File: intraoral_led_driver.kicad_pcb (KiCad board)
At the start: 2 copper layers, 53.8 x 33.2 mm, 248 parts, among them J1 CONN_01X04, J2 CONN_01X03, J3 CONN_01X04, J4 CONN_01X02, J5 CONN_01X02, Q1 Si2318DS-T1, Q2 Si2318DS-T1, SW1 SW_SPST, U1 LT3478-1, U3 AD5247

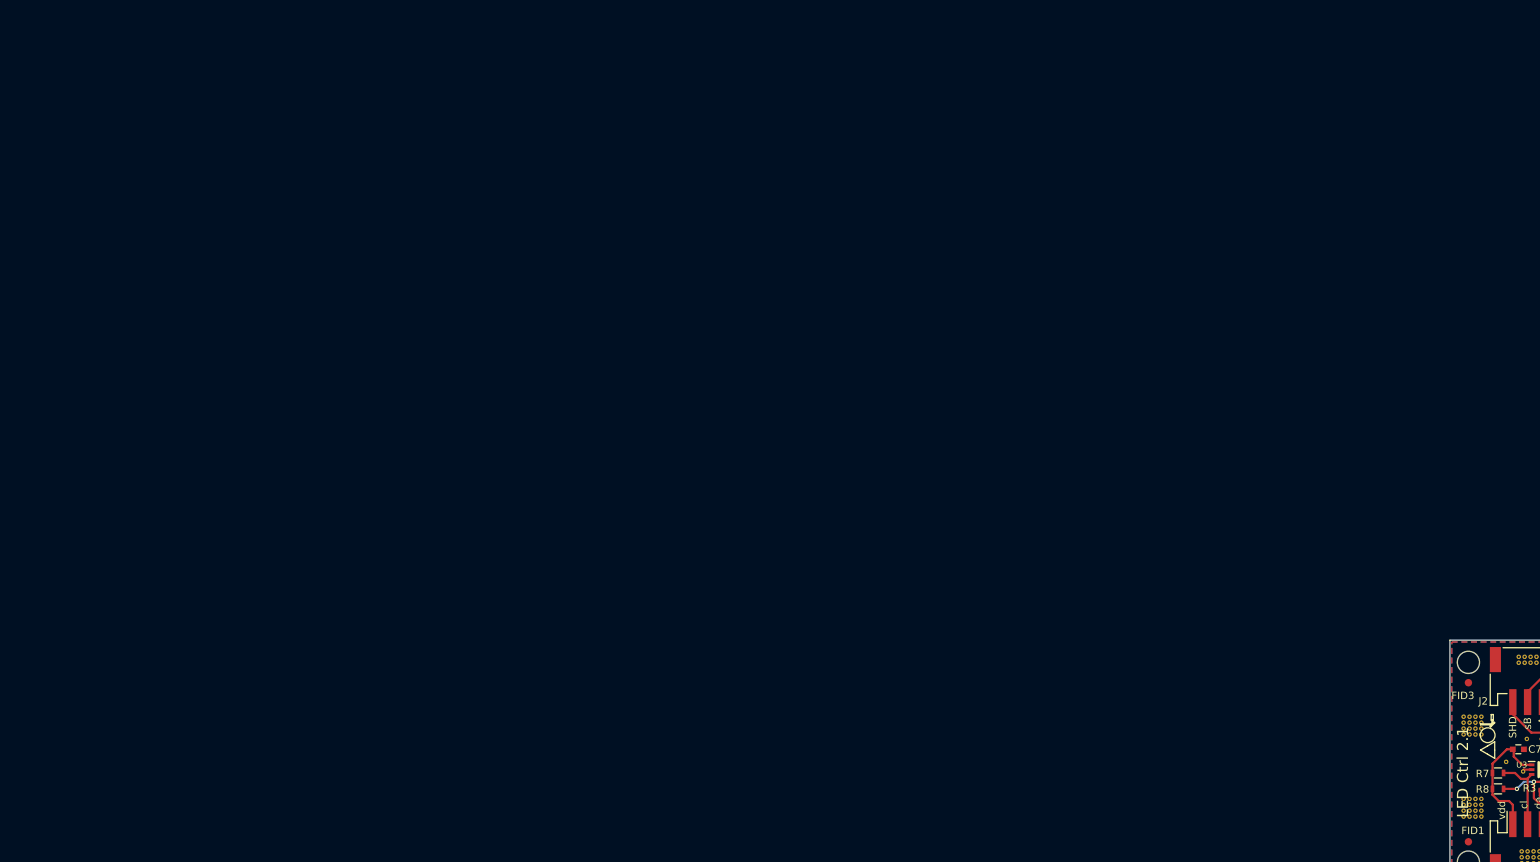
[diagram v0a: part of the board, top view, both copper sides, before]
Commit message: revert version to 1.0 for initial release. remove AOL logo
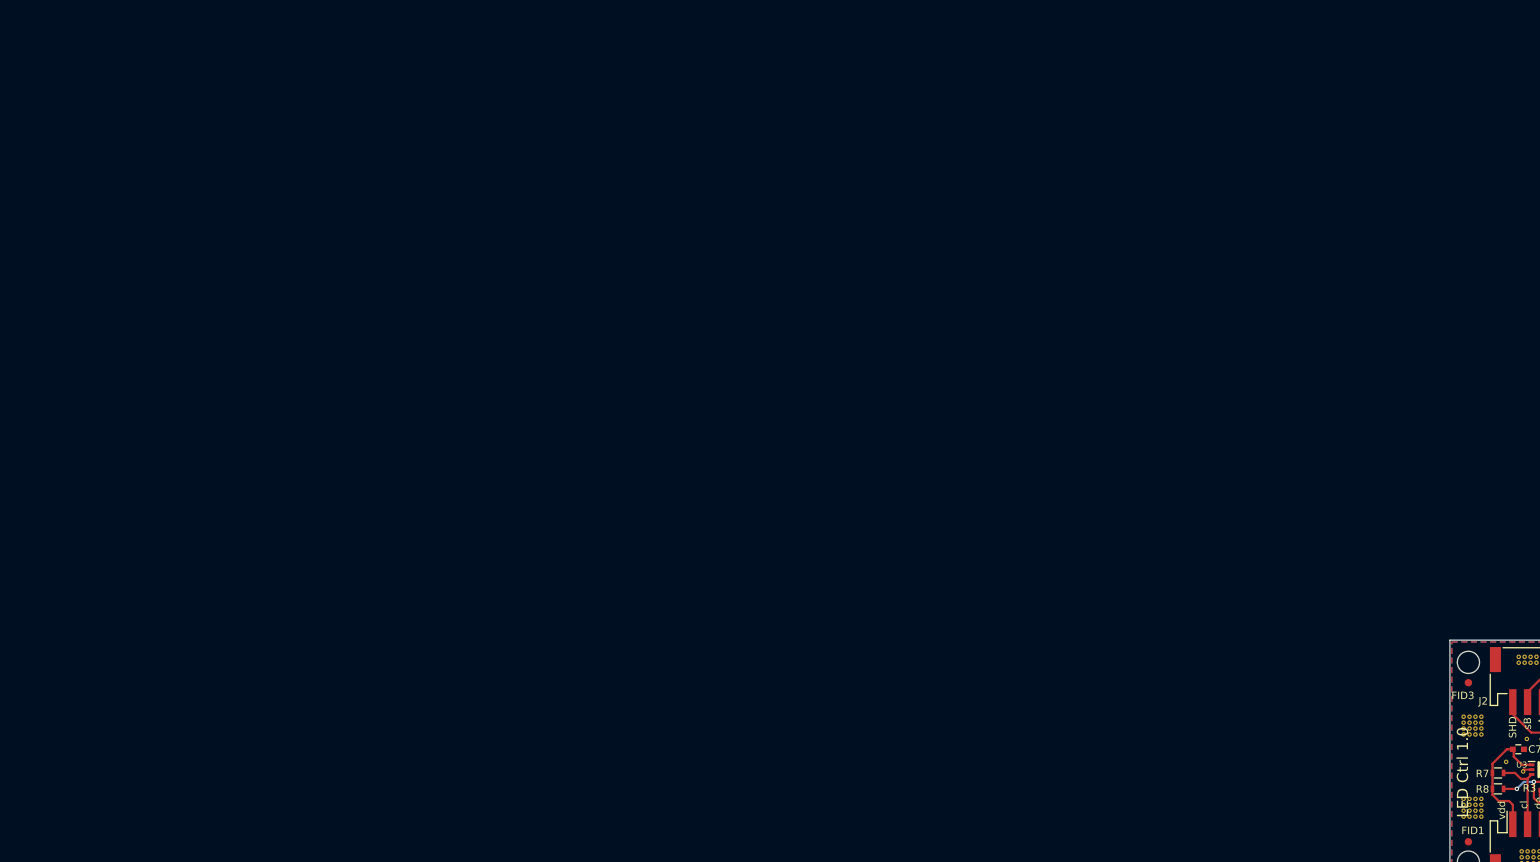
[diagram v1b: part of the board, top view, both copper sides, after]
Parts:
- removed the REF** at (118.5, 127.5)
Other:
- board text added: "LED Ctrl 1.0"
- board text removed: "LED Ctrl 2.1"
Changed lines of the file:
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@@
     (tracks 179)
     (zones 0)
-    (modules 248)
+    (modules 247)
     (nets 24)
   )
@@
     (pad "" np_thru_hole circle (at 0 0) (size 3 3) (drill 3) (layers *.Cu))
   )
-  (module footprints:Logo_AOL (layer F.Cu)
-    (at 118.5 127.5 90)
-    (attr smd)
-    (fp_text reference REF** (at 0 -1.9 90) (layer F.Fab) hide
-      (effects (font (size 1 1) (thickness 0.15)))
-    )
-    (fp_text value Logo_AOL (at 0 1.9 90) (layer F.Fab) hide
-      (effects (font (size 1 1) (thickness 0.15)))
-    )
-    (fp_circle (center -0.6 0.1) (end 0.4 0.1) (layer F.SilkS) (width 0.15))
-    (fp_line (start -3.725942 1.053972) (end -3.166484 0.093498) (layer F.SilkS) (width 0.15))
-    (fp_line (start -3.166484 0.093498) (end -2.607026 -0.866977) (layer F.SilkS) (width 0.15))
-    (fp_line (start -2.607026 -0.866977) (end -2.045931 0.092563) (layer F.SilkS) (width 0.15))
-    (fp_line (start -2.045931 0.092563) (end -1.484836 1.052102) (layer F.SilkS) (width 0.15))
-    (fp_line (start -1.484836 1.052102) (end -2.605389 1.053037) (layer F.SilkS) (width 0.15))
-    (fp_line (start -2.605389 1.053037) (end -3.725942 1.053972) (layer F.SilkS) (width 0.15))
-    (fp_line (start 96.7 -198.9) (end 96.7 -198.9) (layer F.SilkS) (width 0.15))
-    (fp_line (start 0.805121 -0.860085) (end 0.805121 0.609028) (layer F.SilkS) (width 0.15))
-    (fp_line (start 0.805121 0.609028) (end 0.621518 0.425012) (layer F.SilkS) (width 0.15))
-    (fp_line (start 0.621518 0.425012) (end 0.531435 0.514819) (layer F.SilkS) (width 0.15))
-    (fp_line (start 0.531435 0.514819) (end 1.074004 1.058612) (layer F.SilkS) (width 0.15))
-    (fp_line (start 1.074004 1.058612) (end 1.164098 0.968805) (layer F.SilkS) (width 0.15))
-    (fp_line (start 1.164098 0.968805) (end 0.98871 0.79303) (layer F.SilkS) (width 0.15))
-    (fp_line (start 0.98871 0.79303) (end 1.431318 0.79303) (layer F.SilkS) (width 0.15))
-    (fp_line (start 1.431318 0.79303) (end 1.431318 0.865392) (layer F.SilkS) (width 0.15))
-    (fp_line (start 1.431318 0.865392) (end 2.199697 0.865392) (layer F.SilkS) (width 0.15))
-    (fp_line (start 2.199697 0.865392) (end 2.199697 0.577249) (layer F.SilkS) (width 0.15))
-    (fp_line (start 2.199697 0.577249) (end 1.431318 0.577249) (layer F.SilkS) (width 0.15))
-    (fp_line (start 1.431318 0.577249) (end 1.431318 0.664968) (layer F.SilkS) (width 0.15))
-    (fp_line (start 1.431318 0.664968) (end 0.933184 0.664968) (layer F.SilkS) (width 0.15))
-    (fp_line (start 0.933184 0.664968) (end 0.933184 -0.860085) (layer F.SilkS) (width 0.15))
-    (fp_line (start 0.933184 -0.860085) (end 0.805121 -0.860085) (layer F.SilkS) (width 0.15))
-    (fp_line (start 96.6 -198.9) (end 96.6 -198.9) (layer F.SilkS) (width 0.15))
-    (fp_line (start 96.6 -198.9) (end 96.6 -198.9) (layer F.SilkS) (width 0.15))
-  )
   (module TO_SOT_Packages_SMD:SOT-23 (layer F.Cu)
     (at 132.5 123.3)
@@
   )
   (gr_line (start 113.5 115.25) (end 113.5 148.5) (angle 90) (layer Edge.Cuts) (width 0.15))
-  (gr_text "LED Ctrl 2.1\n" (at 115.25 139.25 90) (layer F.SilkS)
+  (gr_text "LED Ctrl 1.0" (at 115.25 139.25 90) (layer F.SilkS)
     (effects (font (size 1.5 1.5) (thickness 0.2)) (justify left))
   )
